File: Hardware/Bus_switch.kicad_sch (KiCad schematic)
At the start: 15 parts, among them J3 Conn_01x04_Pin, U1 SN74CB3Q3384APW

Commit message: changed selected LED resistor from 330 to 1k
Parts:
- removed R1: 330Ω, PCM_JLCPCB:R_0402, symbol PCM_JLCPCB-Resistors:0402,330Ω
- added R12: 1kΩ, PCM_JLCPCB:R_0402, symbol PCM_JLCPCB-Resistors:0402,1kΩ
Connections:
- net SEL1: now also R12.1
- net at D3.1: now also R12.2
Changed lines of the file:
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@@
 	)
 	(symbol
-		(lib_id "PCM_JLCPCB-Resistors:0402,330Ω")
+		(lib_id "PCM_JLCPCB-Resistors:0402,1kΩ")
 		(at 243.84 115.57 0)
 		(unit 1)
@@
 		(dnp no)
 		(fields_autoplaced yes)
-		(property "Reference" "R1"
+		(property "Reference" "R12"
 			(at 246.38 115.5699 0)
 			(show_name no)
@@
 			)
 		)
-		(property "Value" "330Ω"
+		(property "Value" "1kΩ"
 			(at 243.84 115.57 90)
 			(show_name no)
@@
 			)
 		)
-		(property "Datasheet" "https://www.lcsc.com/datasheet/lcsc_datasheet_2205311900_UNI-ROYAL-Uniroyal-Elec-0402WGF3300TCE_C25104.pdf"
-			(at 243.84 115.57 0)
-			(hide yes)
-			(show_name no)
-			(do_not_autoplace no)
-			(effects
-				(font
-					(size 1.27 1.27)
-				)
-			)
-		)
-		(property "Description" "62.5mW Thick Film Resistors 50V ±100ppm/°C ±1% 330Ω 0402 Chip Resistor - Surface Mount ROHS"
-			(at 243.84 115.57 0)
-			(hide yes)
-			(show_name no)
-			(do_not_autoplace no)
-			(effects
-				(font
-					(size 1.27 1.27)
-				)
-			)
-		)
-		(property "LCSC" "C25104"
-			(at 243.84 115.57 0)
-			(hide yes)
-			(show_name no)
-			(do_not_autoplace no)
-			(effects
-				(font
-					(size 1.27 1.27)
-				)
-			)
-		)
-		(property "Stock" "1159127"
+		(property "Datasheet" "https://www.lcsc.com/datasheet/lcsc_datasheet_2206010216_UNI-ROYAL-Uniroyal-Elec-0402WGF1001TCE_C11702.pdf"
+			(at 243.84 115.57 0)
+			(hide yes)
+			(show_name no)
+			(do_not_autoplace no)
+			(effects
+				(font
+					(size 1.27 1.27)
+				)
+			)
+		)
+		(property "Description" "62.5mW Thick Film Resistors 50V ±100ppm/°C ±1% 1kΩ 0402 Chip Resistor - Surface Mount ROHS"
+			(at 243.84 115.57 0)
+			(hide yes)
+			(show_name no)
+			(do_not_autoplace no)
+			(effects
+				(font
+					(size 1.27 1.27)
+				)
+			)
+		)
+		(property "LCSC" "C11702"
+			(at 243.84 115.57 0)
+			(hide yes)
+			(show_name no)
+			(do_not_autoplace no)
+			(effects
+				(font
+					(size 1.27 1.27)
+				)
+			)
+		)
+		(property "Stock" "13226393"
 			(at 243.84 115.57 0)
 			(hide yes)
@@
 			)
 		)
-		(property "Part" "0402WGF3300TCE"
-			(at 243.84 115.57 0)
-			(hide yes)
-			(show_name no)
-			(do_not_autoplace no)
-			(effects
-				(font
-					(size 1.27 1.27)
-				)
-			)
-		)
-		(property "Resistance" "330Ω"
+		(property "Part" "0402WGF1001TCE"
+			(at 243.84 115.57 0)
+			(hide yes)
+			(show_name no)
+			(do_not_autoplace no)
+			(effects
+				(font
+					(size 1.27 1.27)
+				)
+			)
+		)
+		(property "Resistance" "1kΩ"
 			(at 243.84 115.57 0)
 			(hide yes)
@@
 			)
 		)
-		(property "Sim.Device" ""
-			(at 243.84 115.57 0)
-			(hide yes)
-			(show_name no)
-			(do_not_autoplace no)
-			(effects
-				(font
-					(size 1.27 1.27)
-				)
-			)
+		(pin "2"
 		)
 		(pin "1"
-		)
-		(pin "2"
 		)
 		(instances
 			(project "MMS3_hat_templates"
 				(path "/6596548a-44e0-46d8-8624-fd71cf4a3e17/ec6d73af-72b0-4068-85fb-cca3c5143749"
-					(reference "R1")
+					(reference "R12")
 					(unit 1)
 				)

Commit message: changed resistors to 0603
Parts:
- removed R10, R11, R2, R3, R4, R5, R6, R7, R8, R9: 10kΩ, PCM_JLCPCB:R_0402, symbol PCM_JLCPCB-Resistors:0402,10kΩ
- removed R12: 1kΩ, PCM_JLCPCB:R_0402, symbol PCM_JLCPCB-Resistors:0402,1kΩ
- added R1, R10, R2, R3, R4, R5, R6, R7, R8, R9: 10kΩ, PCM_JLCPCB:R_0603, symbol PCM_JLCPCB-Resistors:0603,10kΩ
- added R11: 1kΩ, PCM_JLCPCB:R_0603, symbol PCM_JLCPCB-Resistors:0603,1kΩ
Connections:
- net +3V3: now also R10.1, R3.1, R4.1, R6.1, R7.1, R8.1, R9.1
- net Chainbus.CS: now also R9.2
- net Chainbus.MISO: now also R2.1
- net Chainbus.MOSI: now also R1.1
- net Chainbus.RX: now also R8.2
- net Chainbus.SCK: now also R3.2, R5.1
- net Chainbus.SCL: now also R6.2
- net Chainbus.SDA: now also R10.2
- net Chainbus.TX: now also R7.2
- net GND: now also R1.2, R2.2, R5.2
- net SEL1: now also R11.1, R4.2
- net at D3.1: now also R11.2

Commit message: removed holes from bom
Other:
- company: (none) -> MiniModucard System
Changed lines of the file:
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@@
 	(title_block
 		(title "MMS3 Hat template small (Change Me)")
-		(date "2026-02-25")
+		(date "2077-13-75")
 		(rev "A")
-		(comment 1 "Made by Wojciech Szafrański")
+		(company "MiniModucard System")
+		(comment 1 "Wojciech Szafrański")
 		(comment 2 "Designed in poland")
 	)
@@
 	)
 	(rectangle
-		(start 11.43 27.94)
+		(start 12.7 27.94)
 		(end 86.36 154.94)
 		(stroke
@@
 	(text "Bus Pullups"
 		(exclude_from_sim no)
-		(at 12.7 151.892 0)
+		(at 13.97 151.638 0)
 		(effects
 			(font
@@
 		)
 		(stroke
-			(width 0)
-			(type default)
-		)
-	)
-	(bus
-		(pts
-			(xy 6.35 140.97) (xy 3.81 140.97)
-		)
-		(stroke

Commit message: changed numbering to per-sheet
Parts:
- renumbered C1 to C301, D3 to D301, J3 to J301, R9 to R301, R3 to R302, R5 to R303, R6 to R304, R7 to R305, R8 to R306, R2 to R307, R10 to R308, R1 to R309, R4 to R310, R11 to R311, U1 to U301

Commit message: major rework of template
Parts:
- removed U301: SN74CB3Q3384APW, Package_SO:TSSOP-24_4.4x7.8mm_P0.65mm, symbol 74xx:SN74CB3Q3384APW
- added R312, R313: 0Ω, PCM_JLCPCB:R_0603, symbol PCM_JLCPCB-Resistors:0603,0Ω
- added U302: SN74CB3Q3245PWR, lcsc_footprints:C470961_TSSOP-20_L6_5-W4_4-P0_65-LS6_4-BL, symbol Kicad LCSC Manager:SN74CB3Q3245PWR
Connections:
- net +3V3: now also U302.20 (VCC)
- net Chainbus.CS: now also U302.13 (B6)
- net Chainbus.MISO: now also U302.16 (B3)
- net Chainbus.MOSI: now also U302.15 (B4)
- net Chainbus.RX: now also R312.2
- net Chainbus.SCK: now also U302.14 (B5)
- net Chainbus.SCL: now also U302.12 (B7)
- net Chainbus.SDA: now also U302.11 (B8)
- net Chainbus.TX: now also R313.2
- net Chainbus_In.CS: now also U302.7 (A6)
- net Chainbus_In.MISO: now also U302.4 (A3)
- net Chainbus_In.MOSI: now also U302.5 (A4)
- net Chainbus_In.RX: now also U302.2 (A1)
- net Chainbus_In.SCK: now also U302.6 (A5)
- net Chainbus_In.SCL: now also U302.8 (A7)
- net Chainbus_In.SDA: now also U302.9 (A8)
- net Chainbus_In.TX: now also U302.3 (A2)
- net GND: now also U302.10 (GND)
- net SEL1: now also U302.19 (OE#)
- new net Poka_Yoke_RX: R312.1, U302.18 (B1)
- new net Poka_Yoke_TX: R313.1, U302.17 (B2)
- no-connect marks 4 -> 1
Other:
- note added: "Route As Poka Yoke"

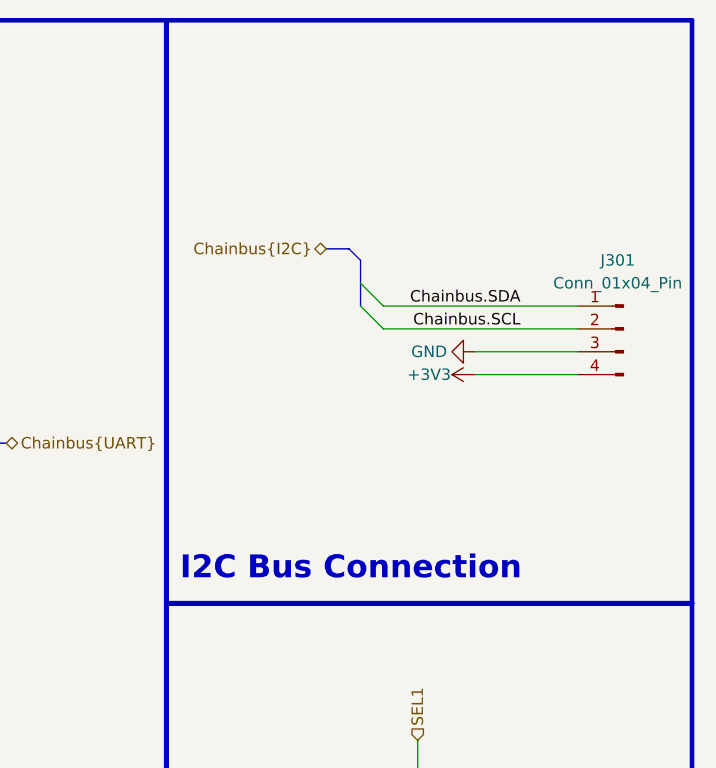
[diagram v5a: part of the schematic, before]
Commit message: connected #WC to GND
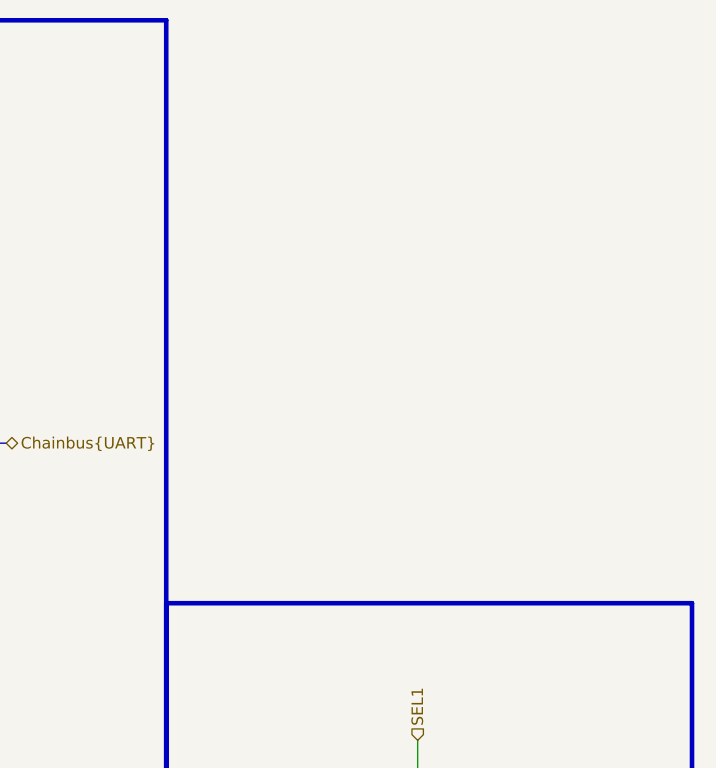
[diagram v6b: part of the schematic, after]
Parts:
- removed J301: Conn_01x04_Pin, Connector_PinHeader_2.54mm:PinHeader_1x04_P2.54mm_Vertical, symbol Connector:Conn_01x04_Pin
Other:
- note removed: "I2C Bus Connection"
